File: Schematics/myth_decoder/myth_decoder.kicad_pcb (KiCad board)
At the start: 2 copper layers, 180 x 100 mm, 35 parts, among them J1 Conn_01x08_Pin, J10 Conn_01x08_Pin, J11 Conn_01x08_Pin, J12 Conn_01x08_Pin, J13 Conn_01x08_Pin, J2 Conn_01x08_Pin, J3 Conn_01x08_Pin, J4 Conn_01x08_Pin, J5 Conn_01x08_Pin, J6 Conn_01x08_Pin, J7 Conn_01x08_Pin, J8 Conn_01x08_Pin, J9 Conn_01x08_Pin, U1 74HC74, U10 74HC238, U11 74HC238, U12 74LS08, U13 74AHC04, U14 4078, U15 4075, U16 74AHC138, U17 74HC238, U18 74AHC138, U19 74AHC138, U2 74LS08, U20 74AHC244, U21 74HC02, U22 74AHC138, U3 74LS32, U4 74HC157, U5 74HC157, U6 74AHC273, U7 74LS148, U8 74AHC138, U9 74HC238

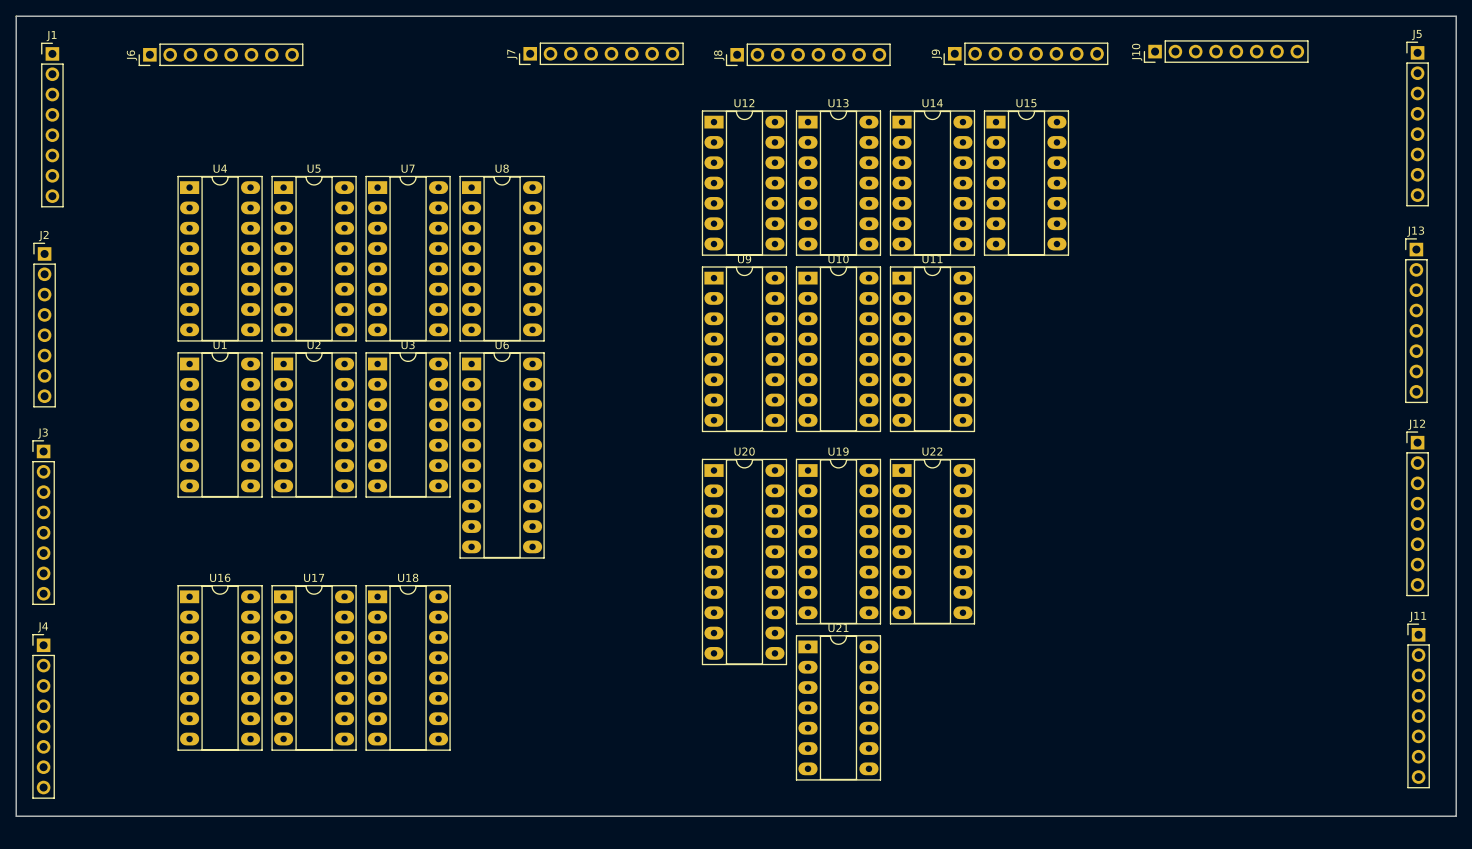
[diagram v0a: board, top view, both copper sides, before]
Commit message: Change d to g
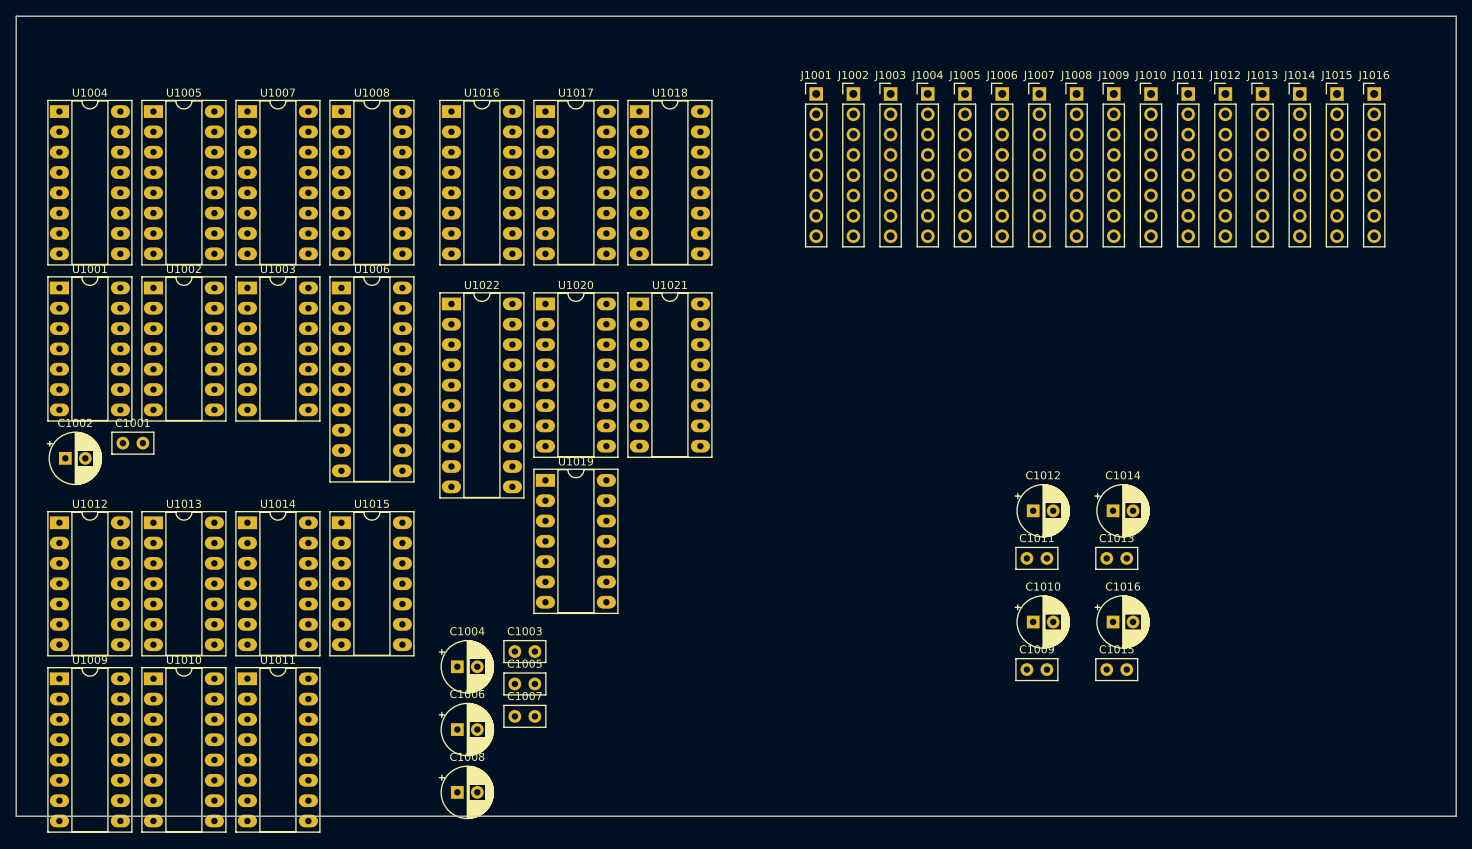
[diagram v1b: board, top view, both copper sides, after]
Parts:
- removed J1, J10, J11, J12, J13, J2, J3, J4, J5, J6, J7, J8, J9: Conn_01x08_Pin, Connector_PinHeader_2.54mm:PinHeader_1x08_P2.54mm_Vertical
- removed U1: 74HC74, Package_DIP:DIP-14_W7.62mm_Socket_LongPads
- removed U10, U11, U17, U9: 74HC238, Package_DIP:DIP-16_W7.62mm_Socket_LongPads
- removed U12, U2: 74LS08, Package_DIP:DIP-14_W7.62mm_Socket_LongPads
- removed U13: 74AHC04, Package_DIP:DIP-14_W7.62mm_Socket_LongPads
- removed U14: 4078, Package_DIP:DIP-14_W7.62mm_Socket_LongPads
- removed U15: 4075, Package_DIP:DIP-14_W7.62mm_Socket_LongPads
- removed U16, U18, U19, U22, U8: 74AHC138, Package_DIP:DIP-16_W7.62mm_Socket_LongPads
- removed U20: 74AHC244, Package_DIP:DIP-20_W7.62mm_Socket_LongPads
- removed U21: 74HC02, Package_DIP:DIP-14_W7.62mm_Socket_LongPads
- removed U3: 74LS32, Package_DIP:DIP-14_W7.62mm_Socket_LongPads
- removed U4, U5: 74HC157, Package_DIP:DIP-16_W7.62mm_Socket_LongPads
- removed U6: 74AHC273, Package_DIP:DIP-20_W7.62mm_Socket_LongPads
- removed U7: 74LS148, Package_DIP:DIP-16_W7.62mm_Socket_LongPads
- added C1001: C 100nF, Capacitor_THT:C_Disc_D5.0mm_W2.5mm_P2.50mm, F.Cu at (36.6, 72.9)
- added C1002: CP 10μF, Capacitor_THT:CP_Radial_D6.3mm_P2.50mm, F.Cu at (29.4, 74.8)
- added C1003: C 100nF, Capacitor_THT:C_Disc_D5.0mm_W2.5mm_P2.50mm, F.Cu at (85.6, 98.9)
- added C1004: CP 10μF, Capacitor_THT:CP_Radial_D6.3mm_P2.50mm, F.Cu at (78.4, 100.8)
- added C1005: C 100nF, Capacitor_THT:C_Disc_D5.0mm_W2.5mm_P2.50mm, F.Cu at (85.6, 103.0)
- added C1006: CP 10μF, Capacitor_THT:CP_Radial_D6.3mm_P2.50mm, F.Cu at (78.4, 108.7)
- added C1007: C 100nF, Capacitor_THT:C_Disc_D5.0mm_W2.5mm_P2.50mm, F.Cu at (85.6, 107.0)
- added C1008: CP 10μF, Capacitor_THT:CP_Radial_D6.3mm_P2.50mm, F.Cu at (78.4, 116.5)
- added C1009: C 100nF, Capacitor_THT:C_Disc_D5.0mm_W2.5mm_P2.50mm, F.Cu at (149.6, 101.2)
- added C1010: CP 10μF, Capacitor_THT:CP_Radial_D6.3mm_P2.50mm, F.Cu at (150.4, 95.2)
- added C1011: C 100nF, Capacitor_THT:C_Disc_D5.0mm_W2.5mm_P2.50mm, F.Cu at (149.6, 87.3)
- added C1012: CP 10μF, Capacitor_THT:CP_Radial_D6.3mm_P2.50mm, F.Cu at (150.4, 81.3)
- added C1013: C 100nF, Capacitor_THT:C_Disc_D5.0mm_W2.5mm_P2.50mm, F.Cu at (159.6, 87.3)
- added C1014: CP 10μF, Capacitor_THT:CP_Radial_D6.3mm_P2.50mm, F.Cu at (160.4, 81.3)
- added C1015: C 100nF, Capacitor_THT:C_Disc_D5.0mm_W2.5mm_P2.50mm, F.Cu at (159.6, 101.2)
- added C1016: CP 10μF, Capacitor_THT:CP_Radial_D6.3mm_P2.50mm, F.Cu at (160.4, 95.2)
- added J1001: Conn_01x08_Pin, Connector_PinHeader_2.54mm:PinHeader_1x08_P2.54mm_Vertical, F.Cu at (123.3, 29.2)
- added J1002: Conn_01x08_Pin, Connector_PinHeader_2.54mm:PinHeader_1x08_P2.54mm_Vertical, F.Cu at (128.0, 29.2)
- added J1003: Conn_01x08_Pin, Connector_PinHeader_2.54mm:PinHeader_1x08_P2.54mm_Vertical, F.Cu at (132.6, 29.2)
- added J1004: Conn_01x08_Pin, Connector_PinHeader_2.54mm:PinHeader_1x08_P2.54mm_Vertical, F.Cu at (137.2, 29.2)
- added J1005: Conn_01x08_Pin, Connector_PinHeader_2.54mm:PinHeader_1x08_P2.54mm_Vertical, F.Cu at (141.9, 29.2)
- added J1006: Conn_01x08_Pin, Connector_PinHeader_2.54mm:PinHeader_1x08_P2.54mm_Vertical, F.Cu at (146.6, 29.2)
- added J1007: Conn_01x08_Pin, Connector_PinHeader_2.54mm:PinHeader_1x08_P2.54mm_Vertical, F.Cu at (151.2, 29.2)
- added J1008: Conn_01x08_Pin, Connector_PinHeader_2.54mm:PinHeader_1x08_P2.54mm_Vertical, F.Cu at (155.8, 29.2)
- added J1009: Conn_01x08_Pin, Connector_PinHeader_2.54mm:PinHeader_1x08_P2.54mm_Vertical, F.Cu at (160.5, 29.2)
- added J1010: Conn_01x08_Pin, Connector_PinHeader_2.54mm:PinHeader_1x08_P2.54mm_Vertical, F.Cu at (165.2, 29.2)
- added J1011: Conn_01x08_Pin, Connector_PinHeader_2.54mm:PinHeader_1x08_P2.54mm_Vertical, F.Cu at (169.8, 29.2)
- added J1012: Conn_01x08_Pin, Connector_PinHeader_2.54mm:PinHeader_1x08_P2.54mm_Vertical, F.Cu at (174.4, 29.2)
- added J1013: Conn_01x08_Pin, Connector_PinHeader_2.54mm:PinHeader_1x08_P2.54mm_Vertical, F.Cu at (179.1, 29.2)
- added J1014: Conn_01x08_Pin, Connector_PinHeader_2.54mm:PinHeader_1x08_P2.54mm_Vertical, F.Cu at (183.8, 29.2)
- added J1015: Conn_01x08_Pin, Connector_PinHeader_2.54mm:PinHeader_1x08_P2.54mm_Vertical, F.Cu at (188.4, 29.2)
- added J1016: Conn_01x08_Pin, Connector_PinHeader_2.54mm:PinHeader_1x08_P2.54mm_Vertical, F.Cu at (193.1, 29.2)
- added U1001: 74HC74, Package_DIP:DIP-14_W7.62mm_Socket_LongPads, F.Cu at (28.7, 53.5)
- added U1002: 74LS08, Package_DIP:DIP-14_W7.62mm_Socket_LongPads, F.Cu at (40.5, 53.5)
- added U1003: 74LS32, Package_DIP:DIP-14_W7.62mm_Socket_LongPads, F.Cu at (52.2, 53.5)
- added U1004: 74HC157, Package_DIP:DIP-16_W7.62mm_Socket_LongPads, F.Cu at (28.7, 31.4)
- added U1005: 74HC157, Package_DIP:DIP-16_W7.62mm_Socket_LongPads, F.Cu at (40.5, 31.4)
- added U1006: 74AHC273, Package_DIP:DIP-20_W7.62mm_Socket_LongPads, F.Cu at (64.0, 53.5)
- added U1007: 74LS148, Package_DIP:DIP-16_W7.62mm_Socket_LongPads, F.Cu at (52.2, 31.4)
- added U1008: 74AHC138, Package_DIP:DIP-16_W7.62mm_Socket_LongPads, F.Cu at (64.0, 31.4)
- added U1009: 74HC238, Package_DIP:DIP-16_W7.62mm_Socket_LongPads, F.Cu at (28.7, 102.3)
- added U1010: 74HC238, Package_DIP:DIP-16_W7.62mm_Socket_LongPads, F.Cu at (40.5, 102.3)
- added U1011: 74HC238, Package_DIP:DIP-16_W7.62mm_Socket_LongPads, F.Cu at (52.2, 102.3)
- added U1012: 74LS08, Package_DIP:DIP-14_W7.62mm_Socket_LongPads, F.Cu at (28.7, 82.8)
- added U1013: 74AHC04, Package_DIP:DIP-14_W7.62mm_Socket_LongPads, F.Cu at (40.5, 82.8)
- added U1014: 4078, Package_DIP:DIP-14_W7.62mm_Socket_LongPads, F.Cu at (52.2, 82.8)
- added U1015: 4075, Package_DIP:DIP-14_W7.62mm_Socket_LongPads, F.Cu at (64.0, 82.8)
- added U1016: 74AHC138, Package_DIP:DIP-16_W7.62mm_Socket_LongPads, F.Cu at (77.7, 31.4)
- added U1017: 74HC238, Package_DIP:DIP-16_W7.62mm_Socket_LongPads, F.Cu at (89.5, 31.4)
- added U1018: 74AHC138, Package_DIP:DIP-16_W7.62mm_Socket_LongPads, F.Cu at (101.2, 31.4)
- added U1019: 74HC02, Package_DIP:DIP-14_W7.62mm_Socket_LongPads, F.Cu at (89.5, 77.5)
- added U1020: 74AHC138, Package_DIP:DIP-16_W7.62mm_Socket_LongPads, F.Cu at (89.5, 55.5)
- added U1021: 74AHC138, Package_DIP:DIP-16_W7.62mm_Socket_LongPads, F.Cu at (101.2, 55.5)
- added U1022: 74AHC244, Package_DIP:DIP-20_W7.62mm_Socket_LongPads, F.Cu at (77.7, 55.5)
